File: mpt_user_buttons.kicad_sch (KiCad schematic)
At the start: 0 parts

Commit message: RTC Finished, changes to User Buttons
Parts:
- added C3: 1uF, symbol Device:C
- added R26: 10k, symbol Device:R
- added SW4: SW_MEC_5E, Button_Switch_THT:SW_NKK_GW12LJP, symbol Switch:SW_MEC_5E
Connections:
- new net +3V4: R26.1
- new net GND: C3.2, SW4.1, SW4.2
- new net GPIO_BUTTON: C3.1, R26.2, SW4.4 (A)
- no-connect marks 0 -> 1
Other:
- note added: "Footprint überprüfen und anpassen Distrelec: 135-66-347"

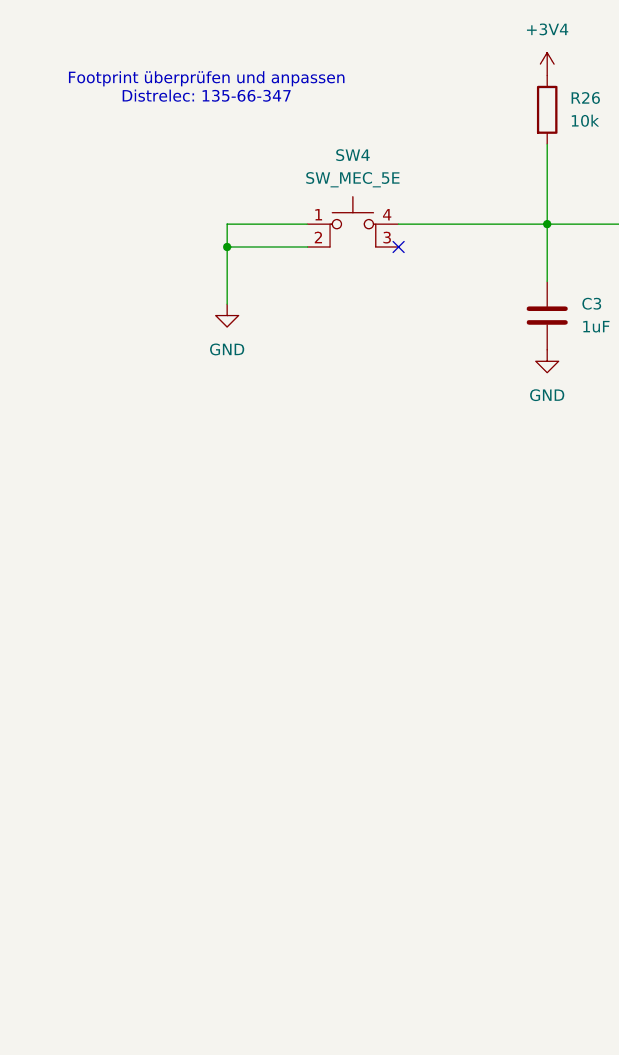
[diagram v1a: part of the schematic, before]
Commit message: Footprints and Symbols for SW, RTC and Joystick
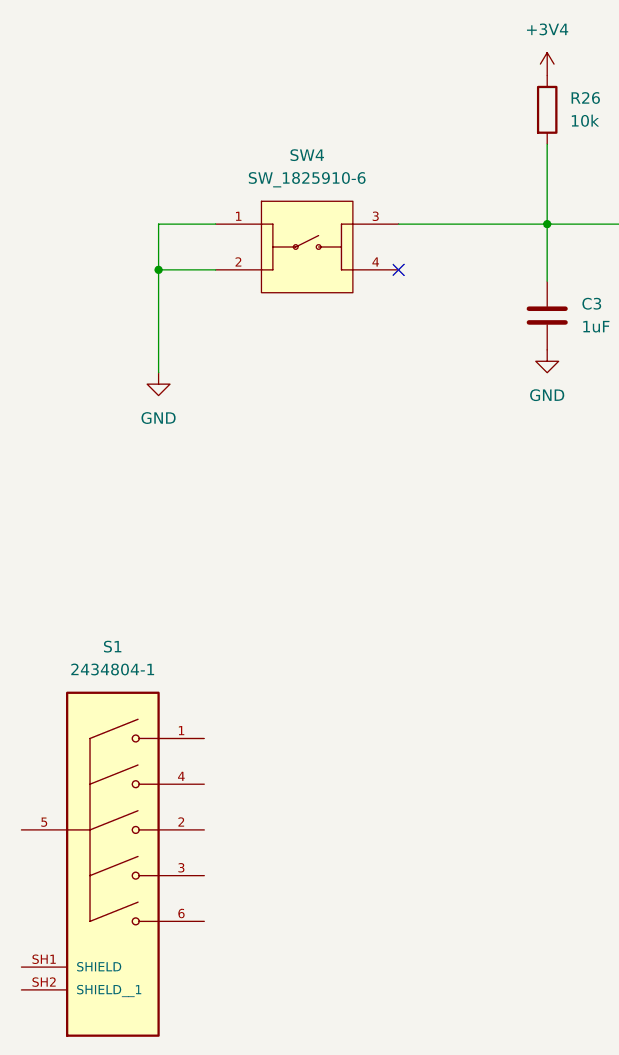
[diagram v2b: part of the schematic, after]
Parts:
- removed SW4: SW_MEC_5E, Button_Switch_THT:SW_NKK_GW12LJP, symbol Switch:SW_MEC_5E
- added S1: 2434804-1, 2434804_1:SW_2434804-1, symbol 2434804-1:2434804-1
- added SW4: SW_1825910-6, 1825910-6:SW_1825910-6-4, symbol MPT_Library:SW_1825910-6
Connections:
- net GND: now also SW4.1, SW4.2
- net GPIO_BUTTON: now also SW4.3
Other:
- note removed: "Footprint überprüfen und anpassen Distrelec: 135-66-347"

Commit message: User Buttons Finished
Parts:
- added C15, C16, C17, C18, C19, C20, C21, C22, C5: 1uF, symbol Device:C
- added R34, R35, R36, R37, R38, R39, R40, R41, R42: 10k, symbol Device:R
- added SW5, SW6, SW7, SW8: SW_1825910-6, 1825910-6:SW_1825910-6-4, symbol MPT_Library:SW_1825910-6
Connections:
- net +3V4: now also R34.1, R35.1, R36.1, R37.1, R38.1, R39.1, R40.1, R41.1, R42.1
- net GND: now also S1.5, S1.SH1 (SHIELD), S1.SH2 (SHIELD__1), C15.2, C16.2, C17.2, C18.2, C19.2, C20.2, C21.2, C22.2, C5.2, SW5.1, SW5.2, SW6.1, SW6.2, SW7.1, SW7.2, SW8.1, SW8.2
- net GPIO_JOYSTICK1: now reaches S1.1
- net GPIO_JOYSTICK1: now also C18.1, R38.2
- net GPIO_JOYSTICK2: now reaches S1.2
- net GPIO_JOYSTICK2: now also C20.1, R40.2
- net GPIO_JOYSTICK3: now reaches S1.3
- net GPIO_JOYSTICK3: now also C21.1, R41.2
- net GPIO_JOYSTICK4: now reaches S1.4
- net GPIO_JOYSTICK4: now also C19.1, R39.2
- net GPIO_JOYSTICK6: now reaches S1.6
- net GPIO_JOYSTICK6: now also C22.1, R42.2
- net GPIO_BUTTON renamed GPIO_BUTTON1
- new net GPIO_BUTTON2: C5.1, R34.2, SW5.3
- new net GPIO_BUTTON3: C15.1, R35.2, SW6.3
- new net GPIO_BUTTON4: C16.1, R36.2, SW7.3
- new net GPIO_BUTTON5: C17.1, R37.2, SW8.3
- no-connect marks 1 -> 5
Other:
- note added: "Button 1"
- note added: "Button 2"
- note added: "Button 3"
- note added: "Joystick"
- moved on the sheet: C3, R26, S1, SW4

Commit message: RTC and User Buttons small changes
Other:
- note added: "Button 4"
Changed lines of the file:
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@@
 		)
 	)
-	(text "Button 3"
+	(text "Button 4\n"
 		(exclude_from_sim no)
 		(at 118.11 79.756 0)
@@
 		)
 	)
-	(text "Button 3"
+	(text "Button 4"
 		(exclude_from_sim no)
 		(at 27.94 79.756 0)

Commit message: Sleep Control Sub-Sheet created, Hirarchy Labels renamed connected
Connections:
- net GPIO_JOYSTICK1 renamed GPIO_JOYSTICK_UP
- net GPIO_JOYSTICK2 renamed GPIO_JOYSTICK_CENTER
- net GPIO_JOYSTICK3 renamed GPIO_JOYSTICK_LEFT
- net GPIO_JOYSTICK4 renamed GPIO_JOYSTICK_RIGHT
- net GPIO_JOYSTICK6 renamed GPIO_JOYSTICK_DOWN
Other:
- note added: "Button 5"
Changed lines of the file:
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@@
 	)
 	(rectangle
-		(start 48.26 130.81)
-		(end 143.51 189.23)
+		(start 50.8 132.08)
+		(end 151.13 190.5)
 		(stroke
 			(width 0)
@@
 		)
 	)
-	(text "Button 4\n"
+	(text "Button 5"
 		(exclude_from_sim no)
 		(at 118.11 79.756 0)
@@
 		)
 	)
-	(hierarchical_label "GPIO_JOYSTICK3"
+	(hierarchical_label "GPIO_JOYSTICK_LEFT"
 		(shape output)
 		(at 125.73 166.37 0)
@@
 		)
 	)
-	(hierarchical_label "GPIO_JOYSTICK6"
+	(hierarchical_label "GPIO_JOYSTICK_DOWN"
 		(shape output)
 		(at 125.73 171.45 0)
@@
 		)
 	)
-	(hierarchical_label "GPIO_JOYSTICK1"
+	(hierarchical_label "GPIO_JOYSTICK_UP"
 		(shape output)
 		(at 125.73 151.13 0)
@@
 		)
 	)
-	(hierarchical_label "GPIO_JOYSTICK2"
+	(hierarchical_label "GPIO_JOYSTICK_CENTER"
 		(shape output)
 		(at 125.73 161.29 0)
@@
 		)
 	)
-	(hierarchical_label "GPIO_JOYSTICK4"
+	(hierarchical_label "GPIO_JOYSTICK_RIGHT"
 		(shape output)
 		(at 125.73 156.21 0)

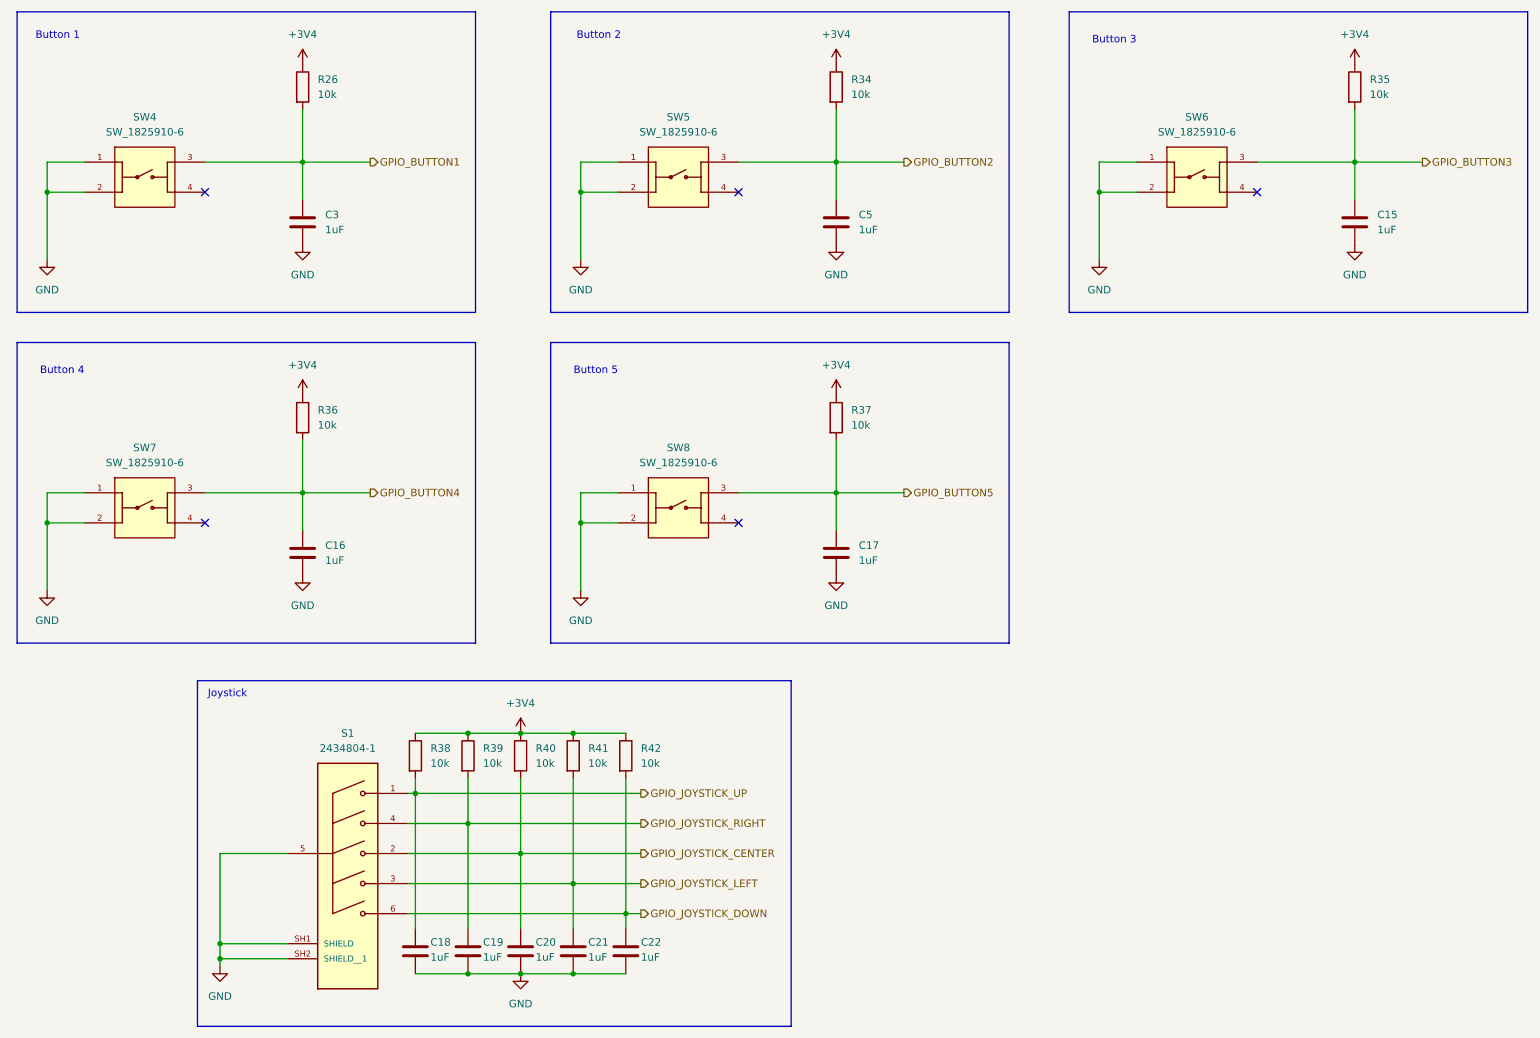
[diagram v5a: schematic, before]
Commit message: Make Block Titles consistent in size Remove not connected marks on mcu for pins which can be used for user buttons and other stuff Add User button hierarchy lables for Button 4 & 5 on MCU sheet Fix hierarchichal pin names on the block not matching the sheet
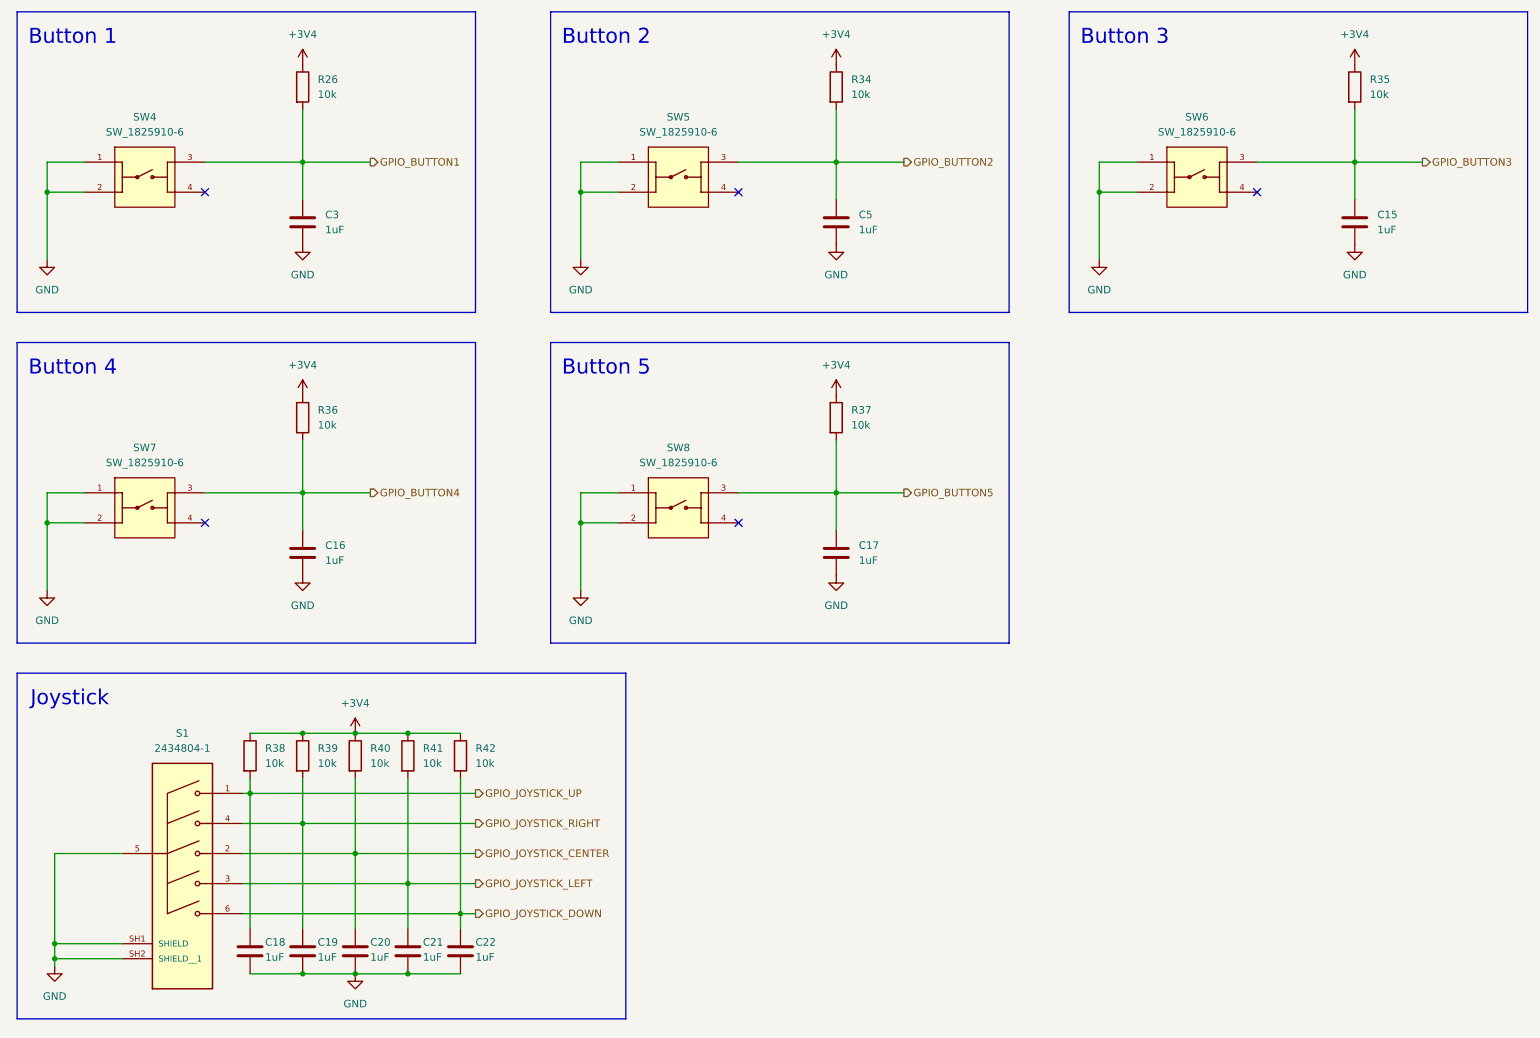
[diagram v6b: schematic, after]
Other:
- moved on the sheet: C18, C19, C20, C21, C22, R38, R39, R40, R41, R42, S1

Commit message: Footprints added, Userbuttons and RTC added on PCB Layout
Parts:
- removed C17: 1uF, symbol Device:C
- removed R37: 10k, symbol Device:R
- removed SW8: SW_1825910-6, 1825910-6:SW_1825910-6-4, symbol MPT_Library:SW_1825910-6
- C15, C16, C18, C19, C20, C21, C22, C3, C5: footprint (none) -> Capacitor_SMD:C_0603_1608Metric
- R26, R34, R35, R36, R38, R39, R40, R41, R42: footprint (none) -> Resistor_SMD:R_0603_1608Metric
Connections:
- no-connect marks 5 -> 4
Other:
- note removed: "Button 5"
- moved on the sheet: C15, C16, R35, R36, SW6, SW7
